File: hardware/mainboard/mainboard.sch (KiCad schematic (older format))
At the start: 28 parts, among them J1 2309407-1, J3 Conn_01x02_Male, J4 AXK7L24223G, J5 503182-1852, U2 MIC5504-1.2YM5-TR, U3 MCP1725-ADJE_MC, U5 ICM-20602

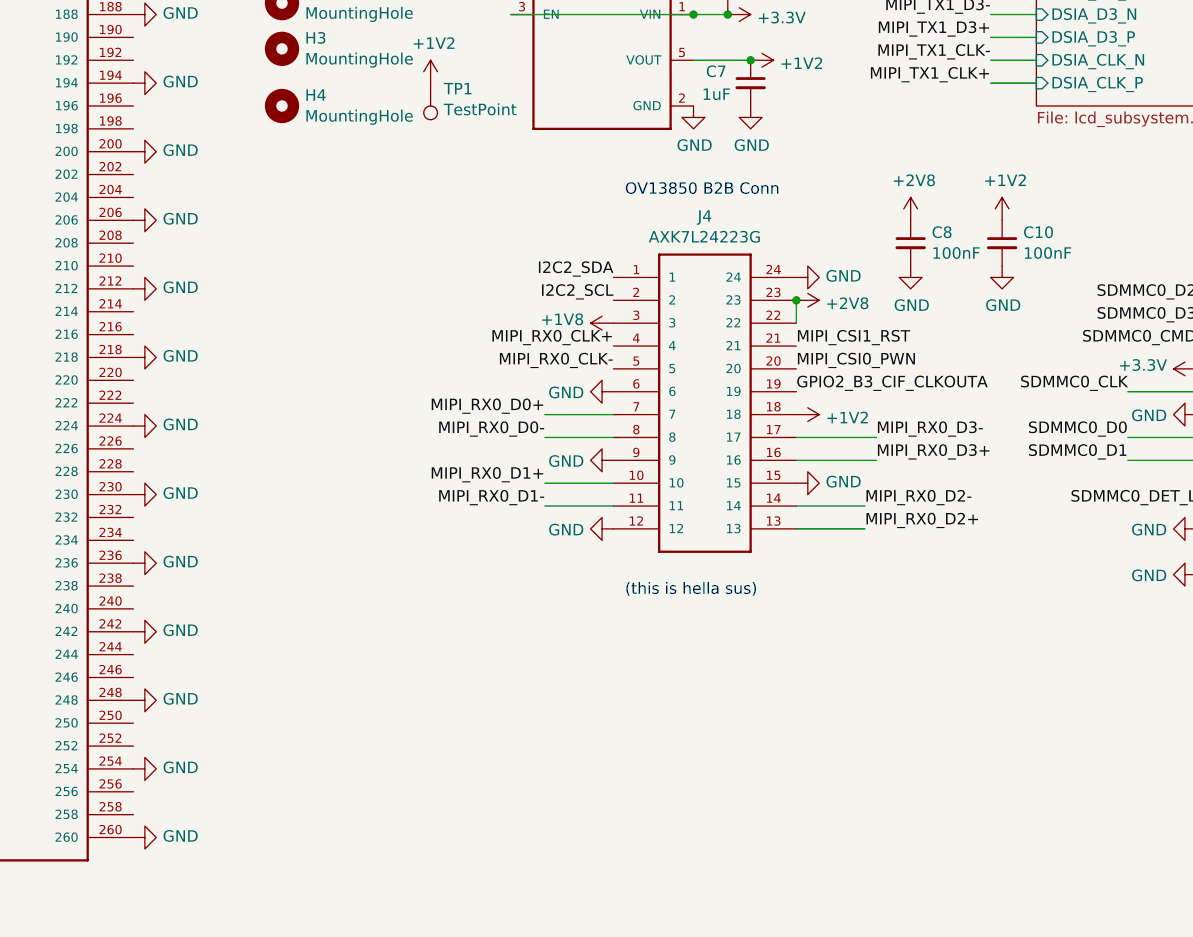
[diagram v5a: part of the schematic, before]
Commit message: add fpc
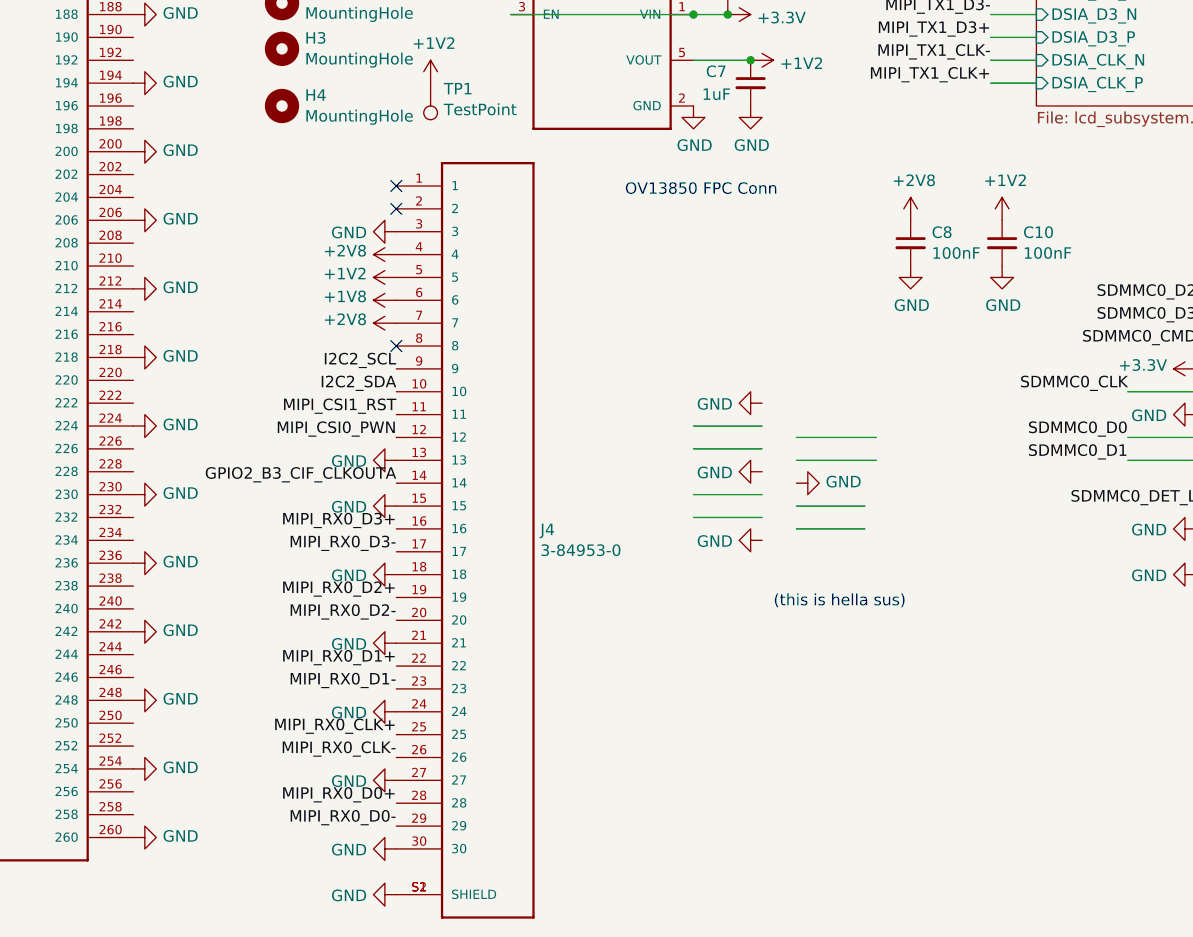
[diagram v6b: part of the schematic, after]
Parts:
- removed J4: AXK7L24223G, mainboard:PANASONIC_AXK7L24223G, symbol mainboard:AXK7L24223G
- added J4: 3-84953-0, mainboard:TE_3-84953-0, symbol mainboard:3-84953-0
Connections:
- wire segments 131 -> 130
- no-connect marks 13 -> 16
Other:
- note added: "OV13850 FPC Conn\n"
- note removed: "OV13850 B2B Conn\n"

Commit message: bugfixes
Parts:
- removed C12: 100nF, Capacitor_SMD:C_0402_1005Metric_Pad0.74x0.62mm_HandSolder, symbol Device:C_Small
- removed H1, H2, H3, H4: MountingHole, MountingHole:MountingHole_2.2mm_M2_Pad_Via, symbol Mechanical:MountingHole
- added H1, H2, H3, H4: MountingHole_Pad, MountingHole:MountingHole_2.2mm_M2_Pad_Via, symbol Mechanical:MountingHole_Pad
- added R3: 1k, Resistor_SMD:R_0402_1005Metric_Pad0.72x0.64mm_HandSolder, symbol Device:R_Small_US
- added R4: 10k, Resistor_SMD:R_0402_1005Metric_Pad0.72x0.64mm_HandSolder, symbol Device:R_Small_US
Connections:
- wire segments 130 -> 125

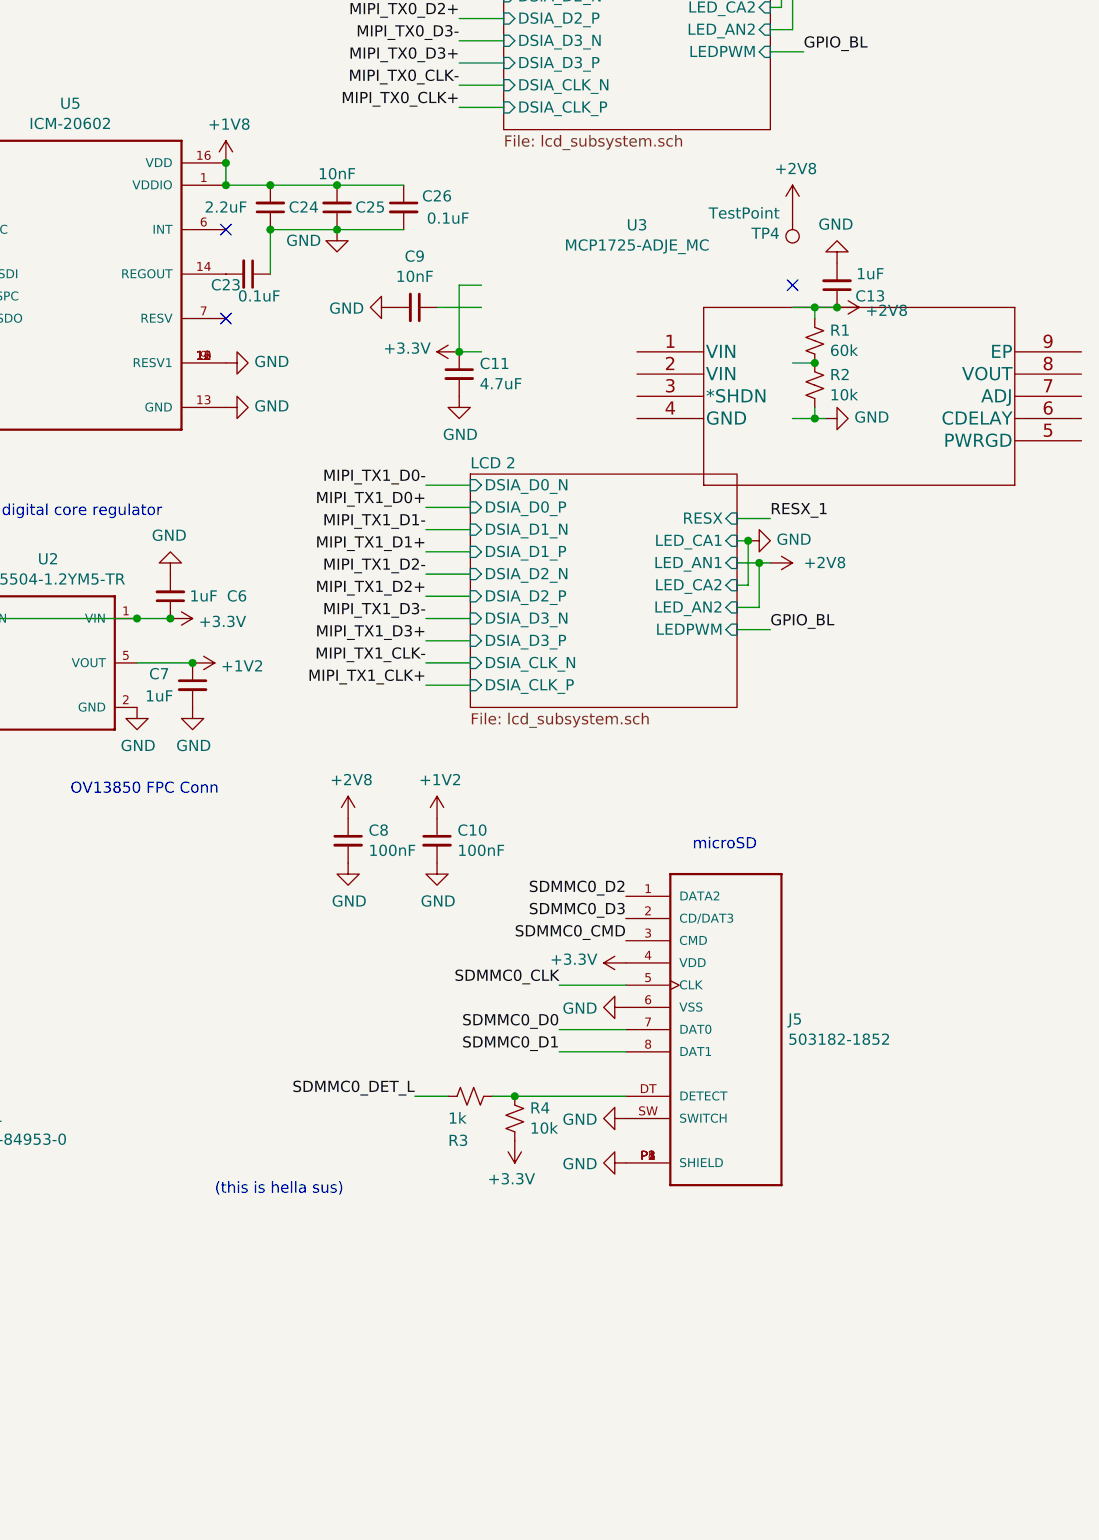
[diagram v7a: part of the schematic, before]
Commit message: 3d models, 1v2 regulator footprint change
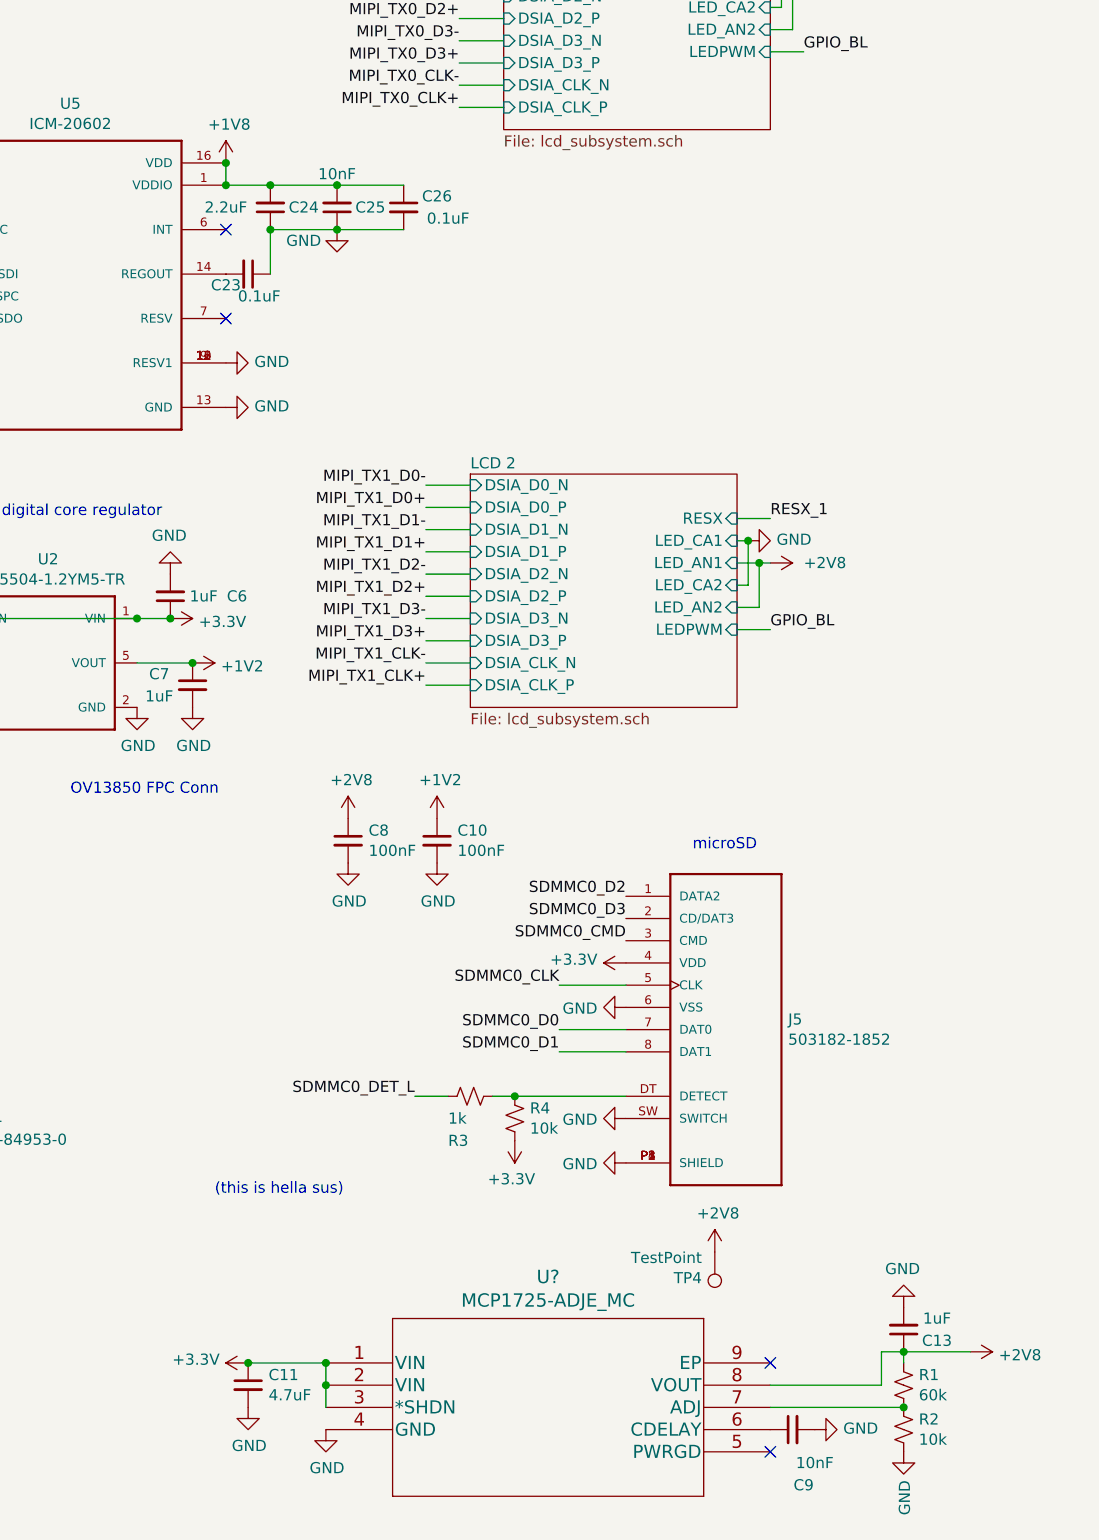
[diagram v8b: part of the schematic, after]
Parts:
- removed U3: MCP1725-ADJE_MC, mainboard:SOIC127P599X175-8N, symbol mainboard:MCP1725-ADJE_MC
- added U?: MCP1725-ADJE_MC, DFN8_2x3MC_MCH, symbol mainboard:MCP1725-ADJE_MC
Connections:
- wire segments 125 -> 123
- no-connect marks 16 -> 17
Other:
- moved on the sheet: C11, C13, C9, R1, R2, TP4
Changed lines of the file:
@@
 EELAYER 30 0
 EELAYER END
-$Descr A4 11693 8268
+$Descr A3 16535 11693
 encoding utf-8
 Sheet 1 3
@@
 $EndComp
 $Comp
-L mainboard:MCP1725-ADJE_MC U3
-U 1 1 5FFFAD28
-P 9900 2600
-F 0 "U3" H 9900 3170 50  0000 C CNN
-F 1 "MCP1725-ADJE_MC" H 9900 3079 50  0000 C CNN
-F 2 "mainboard:SOIC127P599X175-8N" H 9900 2600 50  0001 L BNN
-F 3 "" H 9900 2600 50  0001 C CNN
-	1    9900 2600
-	1    0    0    -1
-$EndComp
-$Comp
 L power:GND #PWR0239
 U 1 1 5FFFC449
-P 10750 2900
-F 0 "#PWR0239" H 10750 2650 50  0001 C CNN
-F 1 "GND" V 10755 2772 50  0000 R CNN
-F 2 "" H 10750 2900 50  0001 C CNN
-F 3 "" H 10750 2900 50  0001 C CNN
-	1    10750 2900
-	0    -1   -1   0
-$EndComp
-$Comp
-L Device:C_Small C9
-U 1 1 60001981
-P 8900 2400
-F 0 "C9" V 8671 2400 50  0000 C CNN
-F 1 "10nF" V 8762 2400 50  0000 C CNN
-F 2 "Capacitor_SMD:C_0402_1005Metric_Pad0.74x0.62mm_HandSolder" H 8900 2400 50  0001 C CNN
-F 3 "~" H 8900 2400 50  0001 C CNN
-	1    8900 2400
-	0    1    1    0
-$EndComp
-Wire Wire Line
-	9000 2400 9200 2400
-$Comp
-L power:GND #PWR0241
-U 1 1 600060D3
-P 8800 2400
-F 0 "#PWR0241" H 8800 2150 50  0001 C CNN
-F 1 "GND" V 8805 2272 50  0000 R CNN
-F 2 "" H 8800 2400 50  0001 C CNN
-F 3 "" H 8800 2400 50  0001 C CNN
-	1    8800 2400
-	0    1    1    0
-$EndComp
-$Comp
-L Device:C_Small C11
-U 1 1 6000EBA4
-P 9100 2700
-F 0 "C11" H 9192 2746 50  0000 L CNN
-F 1 "4.7uF" H 9192 2655 50  0000 L CNN
-F 2 "Capacitor_SMD:C_0402_1005Metric_Pad0.74x0.62mm_HandSolder" H 9100 2700 50  0001 C CNN
-F 3 "~" H 9100 2700 50  0001 C CNN
-	1    9100 2700
-	1    0    0    -1
-$EndComp
-$Comp
-L power:GND #PWR0242
-U 1 1 6001633A
-P 9100 2800
-F 0 "#PWR0242" H 9100 2550 50  0001 C CNN
-F 1 "GND" H 9105 2627 50  0000 C CNN
-F 2 "" H 9100 2800 50  0001 C CNN
-F 3 "" H 9100 2800 50  0001 C CNN
-	1    9100 2800
-	1    0    0    -1
-$EndComp
-Wire Wire Line
-	9200 2300 9100 2300
-Wire Wire Line
-	9100 2300 9100 2600
-Wire Wire Line
-	9100 2600 9200 2600
-Connection ~ 9100 2600
+P 11100 7550
+F 0 "#PWR0239" H 11100 7300 50  0001 C CNN
+F 1 "GND" V 11105 7422 50  0000 R CNN
+F 2 "" H 11100 7550 50  0001 C CNN
+F 3 "" H 11100 7550 50  0001 C CNN
+	1    11100 7550
+	1    0    0    -1
+$EndComp
 $Comp
 L Device:C_Small C13
 U 1 1 60037D5F
-P 10800 2300
-F 0 "C13" H 10650 2350 50  0000 C CNN
-F 1 "1uF" H 10650 2250 50  0000 C CNN
-F 2 "Capacitor_SMD:C_0402_1005Metric_Pad0.74x0.62mm_HandSolder" H 10800 2300 50  0001 C CNN
-F 3 "~" H 10800 2300 50  0001 C CNN
-	1    10800 2300
+P 11100 7000
+F 0 "C13" H 10950 7050 50  0000 C CNN
+F 1 "1uF" H 10950 6950 50  0000 C CNN
+F 2 "Capacitor_SMD:C_0402_1005Metric_Pad0.74x0.62mm_HandSolder" H 11100 7000 50  0001 C CNN
+F 3 "~" H 11100 7000 50  0001 C CNN
+	1    11100 7000
 	-1   0    0    1
 $EndComp
 Wire Wire Line
-	10600 2400 10700 2400
-$Comp
-L power:GND #PWR0243
-U 1 1 60044F35
-P 10800 2200
-F 0 "#PWR0243" H 10800 1950 50  0001 C CNN
-F 1 "GND" H 10805 2027 50  0000 C CNN
-F 2 "" H 10800 2200 50  0001 C CNN
-F 3 "" H 10800 2200 50  0001 C CNN
-	1    10800 2200
-	-1   0    0    1
-$EndComp
+	11000 7100 11100 7100
 $Comp
 L power:+2V8 #PWR0244
 U 1 1 60053149
-P 10800 2400
-F 0 "#PWR0244" H 10800 2250 50  0001 C CNN
-F 1 "+2V8" V 10815 2528 50  0000 L CNN
-F 2 "" H 10800 2400 50  0001 C CNN
-F 3 "" H 10800 2400 50  0001 C CNN
-	1    10800 2400
-	0    1    1    0
-$EndComp
-Connection ~ 10800 2400
+P 11400 7100
+F 0 "#PWR0244" H 11400 6950 50  0001 C CNN
+F 1 "+2V8" V 11415 7228 50  0000 L CNN
+F 2 "" H 11400 7100 50  0001 C CNN
+F 3 "" H 11400 7100 50  0001 C CNN
+	1    11400 7100
+	0    1    1    0
+$EndComp
 Text Label 1450 3500 2    50   ~ 0
 I2C1_SCL
@@
 L Device:R_Small_US R1
 U 1 1 6028A584
-P 10700 2550
-F 0 "R1" H 10768 2596 50  0000 L CNN
-F 1 "60k" H 10768 2505 50  0000 L CNN
-F 2 "Resistor_SMD:R_0402_1005Metric_Pad0.72x0.64mm_HandSolder" H 10700 2550 50  0001 C CNN
-F 3 "~" H 10700 2550 50  0001 C CNN
-	1    10700 2550
+P 11100 7250
+F 0 "R1" H 11168 7296 50  0000 L CNN
+F 1 "60k" H 11168 7205 50  0000 L CNN
+F 2 "Resistor_SMD:R_0402_1005Metric_Pad0.72x0.64mm_HandSolder" H 11100 7250 50  0001 C CNN
+F 3 "~" H 11100 7250 50  0001 C CNN
+	1    11100 7250
 	1    0    0    -1
 $EndComp
@@
 L Device:R_Small_US R2
 U 1 1 6028B549
-P 10700 2750
-F 0 "R2" H 10768 2796 50  0000 L CNN
-F 1 "10k" H 10768 2705 50  0000 L CNN
-F 2 "Resistor_SMD:R_0402_1005Metric_Pad0.72x0.64mm_HandSolder" H 10700 2750 50  0001 C CNN
-F 3 "~" H 10700 2750 50  0001 C CNN
-	1    10700 2750
-	1    0    0    -1
-$EndComp
-Wire Wire Line
-	10600 2650 10700 2650
-Connection ~ 10700 2650
-Wire Wire Line
-	10700 2450 10700 2400
-Connection ~ 10700 2400
-Wire Wire Line
-	10700 2400 10800 2400
-Wire Wire Line
-	10600 2900 10700 2900
-Wire Wire Line
-	10700 2850 10700 2900
-Connection ~ 10700 2900
-Wire Wire Line
-	10700 2900 10750 2900
-NoConn ~ 10600 2300
+P 11100 7450
+F 0 "R2" H 11168 7496 50  0000 L CNN
+F 1 "10k" H 11168 7405 50  0000 L CNN
+F 2 "Resistor_SMD:R_0402_1005Metric_Pad0.72x0.64mm_HandSolder" H 11100 7450 50  0001 C CNN
+F 3 "~" H 11100 7450 50  0001 C CNN
+	1    11100 7450
+	1    0    0    -1
+$EndComp
+Connection ~ 11100 7350
+Wire Wire Line
+	11100 7150 11100 7100
+Connection ~ 11100 7100
 $Comp
 L Connector:Conn_01x02_Male J3
@@
 F 3 "" H 6500 4100 50  0001 C CNN
 	1    6500 4100
-	1    0    0    -1
-$EndComp
-$Comp
-L Connector:TestPoint TP4
-U 1 1 6041ECAA
-P 10600 1950
-F 0 "TP4" H 10658 2068 50  0000 L CNN
-F 1 "TestPoint" H 10658 1977 50  0000 L CNN
-F 2 "TestPoint:TestPoint_Pad_D1.0mm" H 10800 1950 50  0001 C CNN
-F 3 "~" H 10800 1950 50  0001 C CNN
-	1    10600 1950
-	-1   0    0    1
-$EndComp
-$Comp
-L power:+2V8 #PWR0261
-U 1 1 604251F5
-P 10600 1950
-F 0 "#PWR0261" H 10600 1800 50  0001 C CNN
-F 1 "+2V8" H 10615 2123 50  0000 C CNN
-F 2 "" H 10600 1950 50  0001 C CNN
-F 3 "" H 10600 1950 50  0001 C CNN
-	1    10600 1950
 	1    0    0    -1
 $EndComp
@@
 Text Label 8950 3600 2    50   ~ 0
 MIPI_TX1_D2-
-$Comp
-L power:+3.3V #PWR0240
-U 1 1 5F959D72
-P 9100 2600
-F 0 "#PWR0240" H 9100 2450 50  0001 C CNN
-F 1 "+3.3V" V 9115 2728 50  0000 L CNN
-F 2 "" H 9100 2600 50  0001 C CNN
-F 3 "" H 9100 2600 50  0001 C CNN
-	1    9100 2600
-	0    -1   -1   0
-$EndComp
 $Comp
 L power:+3.3V #PWR0254
@@
 $EndComp
 $Comp
-L power:+3.3V #PWR?
+L power:+3.3V #PWR0234
 U 1 1 5F9D2351
 P 2750 4600
-F 0 "#PWR?" H 2750 4450 50  0001 C CNN
+F 0 "#PWR0234" H 2750 4450 50  0001 C CNN
 F 1 "+3.3V" V 2765 4728 50  0000 L CNN
 F 2 "" H 2750 4600 50  0001 C CNN
@@
 	0    1    1    0
 $EndComp
+$Comp
+L power:GND #PWR0242
+U 1 1 6001633A
+P 8150 7350
+F 0 "#PWR0242" H 8150 7100 50  0001 C CNN
+F 1 "GND" H 8155 7177 50  0000 C CNN
+F 2 "" H 8150 7350 50  0001 C CNN
+F 3 "" H 8150 7350 50  0001 C CNN
+	1    8150 7350
+	1    0    0    -1
+$EndComp
+$Comp
+L Device:C_Small C11
+U 1 1 6000EBA4
+P 8150 7250
+F 0 "C11" H 8242 7296 50  0000 L CNN
+F 1 "4.7uF" H 8242 7205 50  0000 L CNN
+F 2 "Capacitor_SMD:C_0402_1005Metric_Pad0.74x0.62mm_HandSolder" H 8150 7250 50  0001 C CNN
+F 3 "~" H 8150 7250 50  0001 C CNN
+	1    8150 7250
+	1    0    0    -1
+$EndComp
+$Comp
+L power:+2V8 #PWR0261
+U 1 1 604251F5
+P 10250 6650
+F 0 "#PWR0261" H 10250 6500 50  0001 C CNN
+F 1 "+2V8" H 10265 6823 50  0000 C CNN
+F 2 "" H 10250 6650 50  0001 C CNN
+F 3 "" H 10250 6650 50  0001 C CNN
+	1    10250 6650
+	1    0    0    -1
+$EndComp
+$Comp
+L Connector:TestPoint TP4
+U 1 1 6041ECAA
+P 10250 6650
+F 0 "TP4" H 10308 6768 50  0000 L CNN
+F 1 "TestPoint" H 10308 6677 50  0000 L CNN
+F 2 "TestPoint:TestPoint_Pad_D1.0mm" H 10450 6650 50  0001 C CNN
+F 3 "~" H 10450 6650 50  0001 C CNN
+	1    10250 6650
+	-1   0    0    1
+$EndComp
+NoConn ~ 10500 7550
+NoConn ~ 10500 7150
+$Comp
+L power:GND #PWR?
+U 1 1 5FA58E8D
+P 8500 7450
+F 0 "#PWR?" H 8500 7200 50  0001 C CNN
+F 1 "GND" H 8505 7277 50  0000 C CNN
+F 2 "" H 8500 7450 50  0001 C CNN
+F 3 "" H 8500 7450 50  0001 C CNN
+	1    8500 7450
+	1    0    0    -1
+$EndComp
+Wire Wire Line
+	8500 7250 8500 7350
+Connection ~ 8500 7250
+Wire Wire Line
+	8500 7150 8500 7250
+$Comp
+L mainboard:MCP1725-ADJE_MC U?
+U 1 1 5F9F70E9
+P 8500 7150
+F 0 "U?" H 9500 7537 60  0000 C CNN
+F 1 "MCP1725-ADJE_MC" H 9500 7431 60  0000 C CNN
+F 2 "DFN8_2x3MC_MCH" H 9500 7390 60  0001 C CNN
+F 3 "" H 8500 7150 60  0000 C CNN
+	1    8500 7150
+	1    0    0    -1
+$EndComp
+$Comp
+L power:GND #PWR0241
+U 1 1 600060D3
+P 10700 7450
+F 0 "#PWR0241" H 10700 7200 50  0001 C CNN
+F 1 "GND" V 10705 7322 50  0000 R CNN
+F 2 "" H 10700 7450 50  0001 C CNN
+F 3 "" H 10700 7450 50  0001 C CNN
+	1    10700 7450
+	0    -1   -1   0
+$EndComp
+$Comp
+L Device:C_Small C9
+U 1 1 60001981
+P 10600 7450
+F 0 "C9" V 10350 7400 50  0000 C CNN
+F 1 "10nF" V 10450 7350 50  0000 C CNN
+F 2 "Capacitor_SMD:C_0402_1005Metric_Pad0.74x0.62mm_HandSolder" H 10600 7450 50  0001 C CNN
+F 3 "~" H 10600 7450 50  0001 C CNN
+	1    10600 7450
+	0    -1   -1   0
+$EndComp
+$Comp
+L power:+3.3V #PWR?
+U 1 1 5FB39ABE
+P 8150 7150
+F 0 "#PWR?" H 8150 7000 50  0001 C CNN
+F 1 "+3.3V" V 8165 7278 50  0000 L CNN
+F 2 "" H 8150 7150 50  0001 C CNN
+F 3 "" H 8150 7150 50  0001 C CNN
+	1    8150 7150
+	0    -1   -1   0
+$EndComp
+Wire Wire Line
+	8150 7150 8500 7150
+Connection ~ 8150 7150
+Connection ~ 8500 7150
+Wire Wire Line
+	10500 7350 11100 7350
+Wire Wire Line
+	10500 7250 11000 7250
+Wire Wire Line
+	11000 7250 11000 7100
+Wire Wire Line
+	11100 7100 11400 7100
+$Comp
+L power:GND #PWR?
+U 1 1 5FBE8000
+P 11100 6900
+F 0 "#PWR?" H 11100 6650 50  0001 C CNN
+F 1 "GND" H 11105 6727 50  0000 C CNN
+F 2 "" H 11100 6900 50  0001 C CNN
+F 3 "" H 11100 6900 50  0001 C CNN
+	1    11100 6900
+	-1   0    0    1
+$EndComp
 $EndSCHEMATC
